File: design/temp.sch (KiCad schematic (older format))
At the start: 3 parts

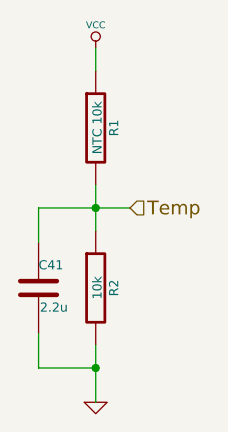
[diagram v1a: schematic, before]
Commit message: Make change in annotations and some small fixes
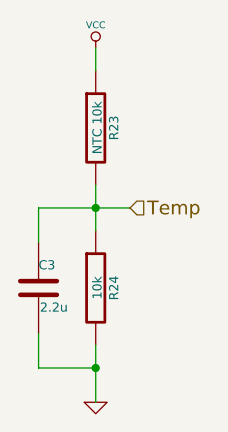
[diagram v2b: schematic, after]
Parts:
- renumbered C41 to C3, R1 to R23, R2 to R24
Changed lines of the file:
@@
 $Descr A4 11693 8268
 encoding utf-8
-Sheet 3 11
+Sheet 3 10
 Title "NTC resistor temperature sensor"
-Date "13 jan 2015"
+Date "16 jan 2015"
 Rev ""
 Comp "Mrk Industries"
@@
 $EndDescr
 $Comp
-L R R1
+L R R23
 U 1 1 5426DA2F
 P 4400 3400
-F 0 "R1" V 4480 3400 40  0000 C CNN
+F 0 "R23" V 4480 3400 40  0000 C CNN
 F 1 "NTC 10k" V 4407 3401 40  0000 C CNN
 F 2 "SMD_Packages:SMD-0603_r" V 4330 3400 30  0001 C CNN
@@
 $EndComp
 $Comp
-L R R2
+L R R24
 U 1 1 5426DAA6
 P 4400 4100
-F 0 "R2" V 4480 4100 40  0000 C CNN
+F 0 "R24" V 4480 4100 40  0000 C CNN
 F 1 "10k" V 4407 4101 40  0000 C CNN
 F 2 "SMD_Packages:SMD-0603_r" V 4330 4100 30  0001 C CNN
@@
 $EndComp
 $Comp
-L C C41
+L C C3
 U 1 1 5426DADD
 P 4150 4100
-F 0 "C41" H 4150 4200 40  0000 L CNN
+F 0 "C3" H 4150 4200 40  0000 L CNN
 F 1 "2.2u" H 4156 4015 40  0000 L CNN
 F 2 "SMD_Packages:SMD-0603_c" H 4188 3950 30  0001 C CNN
@@
 $EndComp
 $Comp
-L VCC #PWR023
+L VCC #PWR028
 U 1 1 5426DB11
 P 4400 3050
-F 0 "#PWR023" H 4400 3150 30  0001 C CNN
+F 0 "#PWR028" H 4400 3150 30  0001 C CNN
 F 1 "VCC" H 4400 3150 30  0000 C CNN
 F 2 "" H 4400 3050 60  0000 C CNN
@@
 $EndComp
 $Comp
-L GND #PWR024
+L GND #PWR029
 U 1 1 5426DB25
 P 4400 4600
-F 0 "#PWR024" H 4400 4600 30  0001 C CNN
+F 0 "#PWR029" H 4400 4600 30  0001 C CNN
 F 1 "GND" H 4400 4530 30  0001 C CNN
 F 2 "" H 4400 4600 60  0000 C CNN
